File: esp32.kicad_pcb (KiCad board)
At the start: 2 copper layers, 25.4 x 41.8 mm, 21 parts, among them IC1 ESP32-WROVER-E_M213EH6464PH3Q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, J1 Micro_SD_Card_Det, J4 Bus_Connector, U1 MCP2518FDT-H_SL, U2 SN65HVD231, U3 SRV05-4, Y1 XRCGB40M000F4M02R0

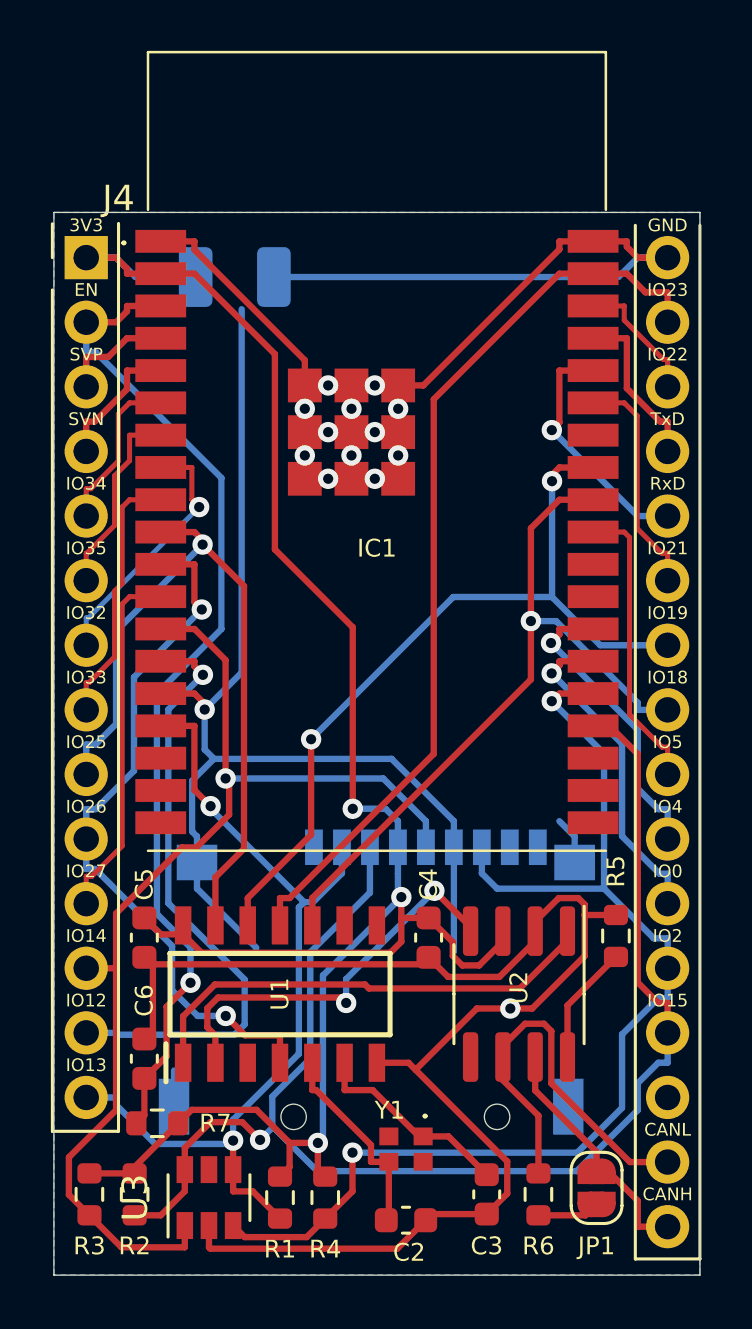
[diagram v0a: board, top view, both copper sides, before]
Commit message: Footprints für "Hand solder" Wahlweise MCP2518 oder interner CAN
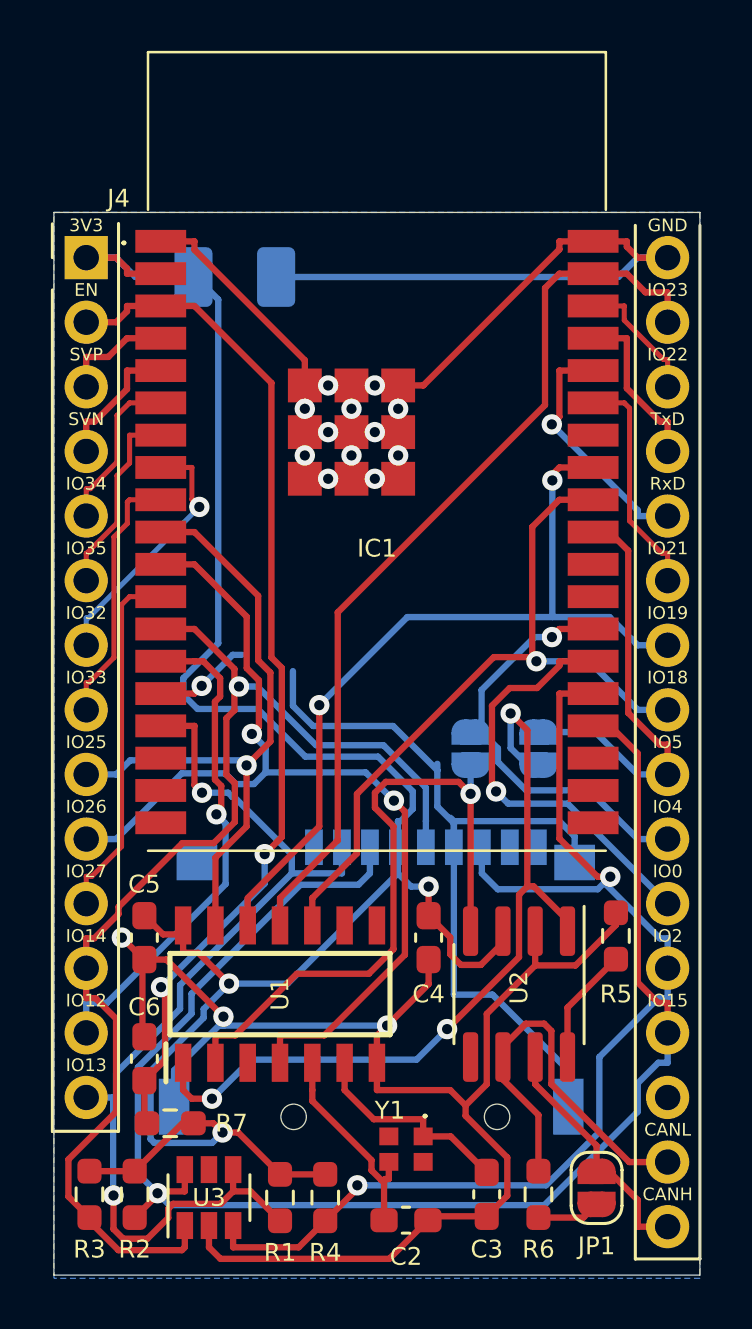
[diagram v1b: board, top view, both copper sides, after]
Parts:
- added JP2: SolderJumper_2_Open, Jumper:SolderJumper-2_P1.3mm_Open_RoundedPad1.0x1.5mm, B.Cu at (104.1, 85.3)
- added JP3: SolderJumper_2_Open, Jumper:SolderJumper-2_P1.3mm_Open_RoundedPad1.0x1.5mm, B.Cu at (101.5, 85.3)
- C1: footprint Capacitor_Tantalum_SMD:CP_EIA-3528-21_Kemet-B -> Capacitor_Tantalum_SMD:CP_EIA-3528-21_Kemet-B_Pad1.50x2.35mm_HandSolder
- C2, C3, C4, C5, C6: footprint Capacitor_SMD:C_0603_1608Metric -> Capacitor_SMD:C_0603_1608Metric_Pad1.08x0.95mm_HandSolder
- R1, R2, R3, R4, R5, R6, R7: footprint Resistor_SMD:R_0603_1608Metric -> Resistor_SMD:R_0603_1608Metric_Pad0.98x0.95mm_HandSolder
- moved R7 0.51 mm to (89.7, 100.1)
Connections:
- net Net-(IC1-Pad26) renamed IO4
- net Net-(IC1-Pad29) renamed IO5
- net Net-(U1-Pad1) renamed TXCAN
- net Net-(U1-Pad2) renamed RXCAN
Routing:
- net GND: track 166.0 -> 147.7 mm, vias 14 -> 16
- net TXCAN: track 18.7 -> 32.0 mm, vias 0 -> 3
- net RXCAN: track 16.0 -> 26.6 mm, vias 2 -> 1
- net MCP_INT: track 27.9 -> 38.4 mm
- net SD_CMD: track 54.7 -> 60.6 mm
- net IO5: track 11.6 -> 17.1 mm
- net IO4: track 11.8 -> 16.9 mm
- net SD_DAT3: track 34.6 -> 39.4 mm
- net Net-(IC1-Pad14): track 24.0 -> 19.7 mm
- net IO0: track 13.1 -> 16.8 mm
- net MCP_CS: track 29.2 -> 25.5 mm
- net SD_CLK: track 44.1 -> 47.3 mm
- net EN: track 39.7 -> 40.6 mm, vias 1 -> 2
- net MCP_MISO: track 32.0 -> 32.7 mm
- net +3V3: track 81.4 -> 81.9 mm
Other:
- board text added: "Closed = Int. CAN No MCP2518"
